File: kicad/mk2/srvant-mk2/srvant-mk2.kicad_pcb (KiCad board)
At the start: 4 copper layers, 104.8 x 158.5 mm, 241 parts, among them J1 Barrel_Jack_Switch, J10 HDMI connector, J11 USB A, J2 Conn_01x02, J3 Conn_01x03, J4 USB_OTG, J5 ARJM11, J8 Bus_M.2_Socket_M, J9 ARJM11, Q1 DMP3013SFV-7, SW1 POWER, SW2 EMMC_KEY, SW3 RST, SW4 HOST_RESET, U1 AP63205WU, U10 TPD4EUSB30, U11 TPD4EUSB30, U12 KSZ9131RNXI-TR, U13 74AHC1G04, U14 AP22653W6, U15 TLV62585DRLR, U16 FSUSB42MUX, U17 PCF85063AT/AAZ, U18 74LVC1G07SE-7, U19 TPD4EUSB30, U2 AP64501SP-13, U20 TPD4EUSB30, U21 74LVC1G07SE-7, U22 TMP1075DSG, U23 SLB9670VQ20FW785XTMA1, U24 74AHC1G08, U25 74AHC1G08, U3 74AHC1G32, U4 INA219AxDCN, U5 rp-t113-s3, U6 PCF85063AT/AAZ, U7 TPD4EUSB30, U8 74LVC2G07, U9 RT9742SNGV, Y1 X32K768S301, Y2 25Mhz, Y3 X32K768S301

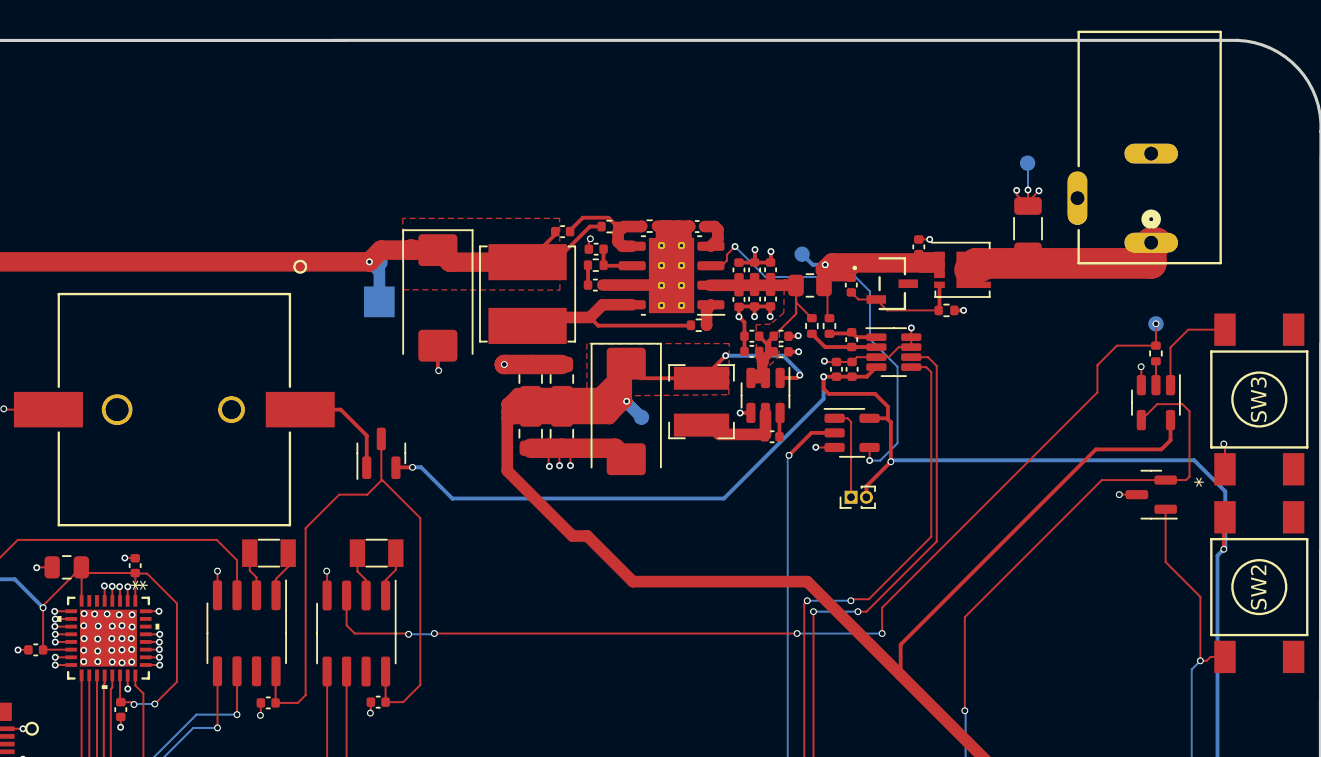
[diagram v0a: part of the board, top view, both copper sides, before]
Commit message: fix descriptions, add 3dmodels.
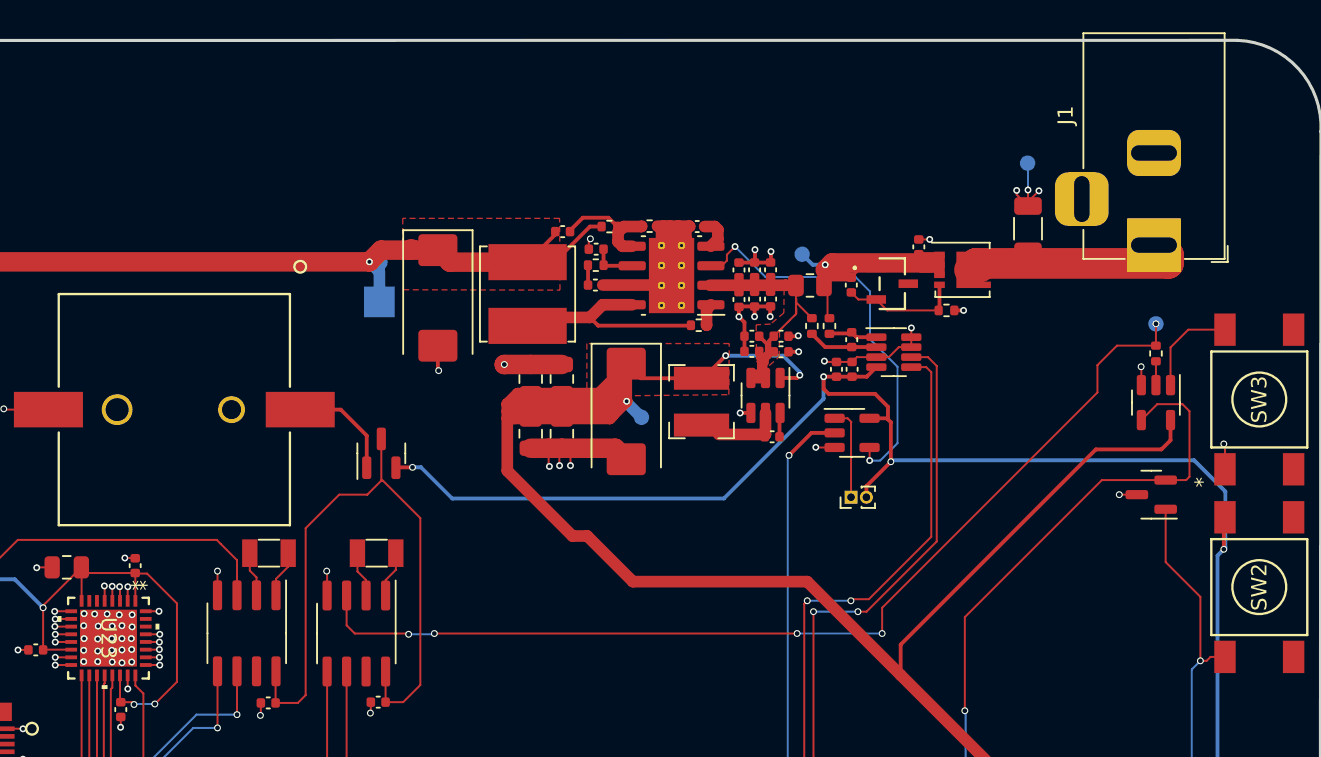
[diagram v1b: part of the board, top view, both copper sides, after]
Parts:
- J1: footprint footprints:DC-jack-694106301002 -> Connector_BarrelJack:BarrelJack_Horizontal
- SW4: value HOST_RESET -> RESET
- moved J1 0.24 mm to (105.9, 52.9)
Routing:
- net Net-(Q1-D): track 14.2 -> 15.3 mm

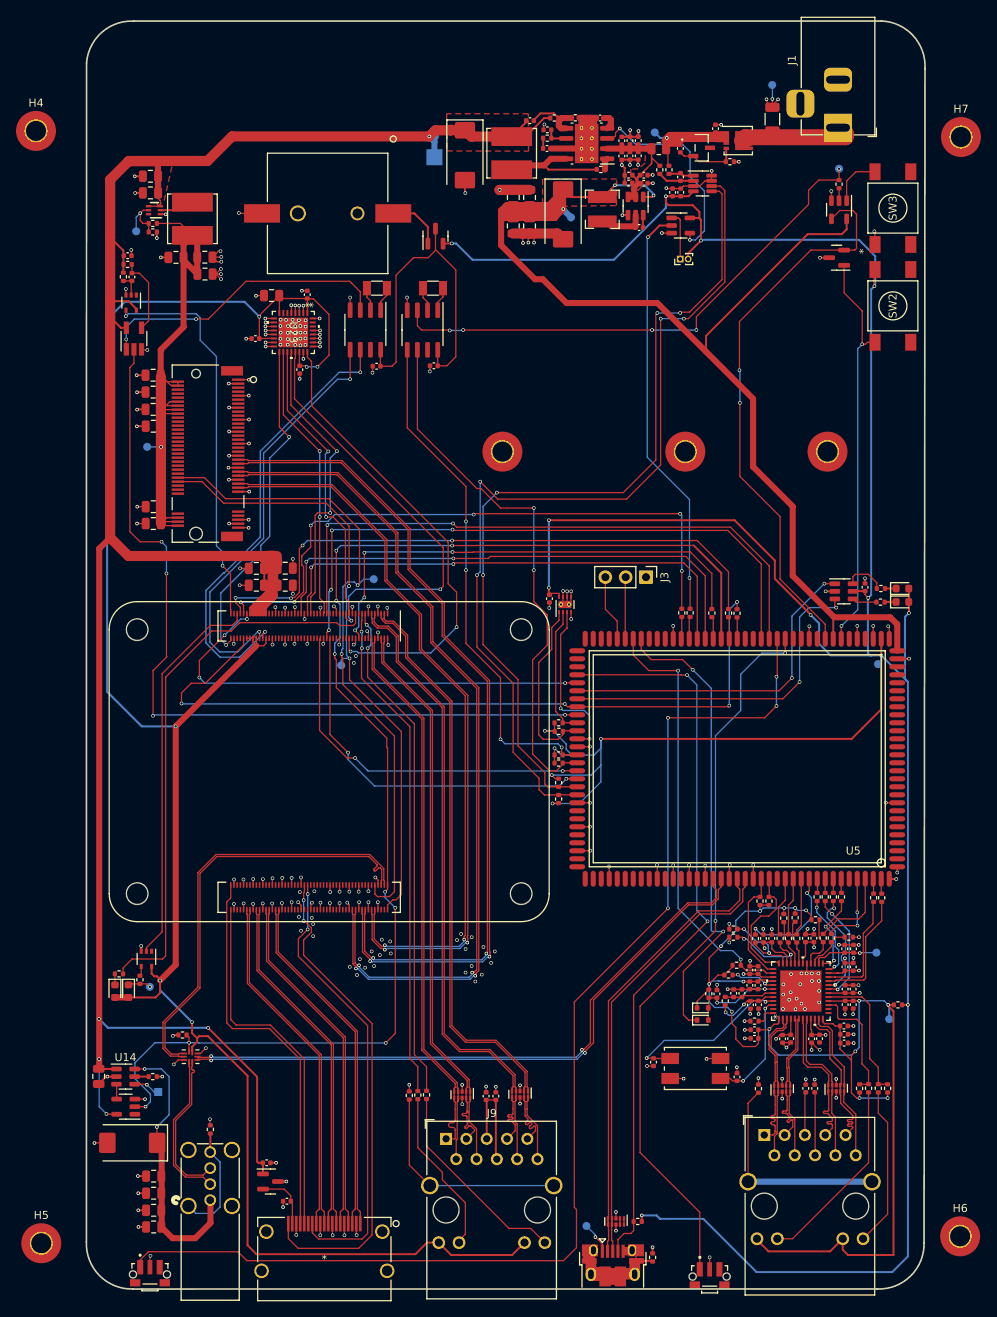
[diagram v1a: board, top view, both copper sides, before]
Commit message: replace power jack, change board dimentions, small fixes
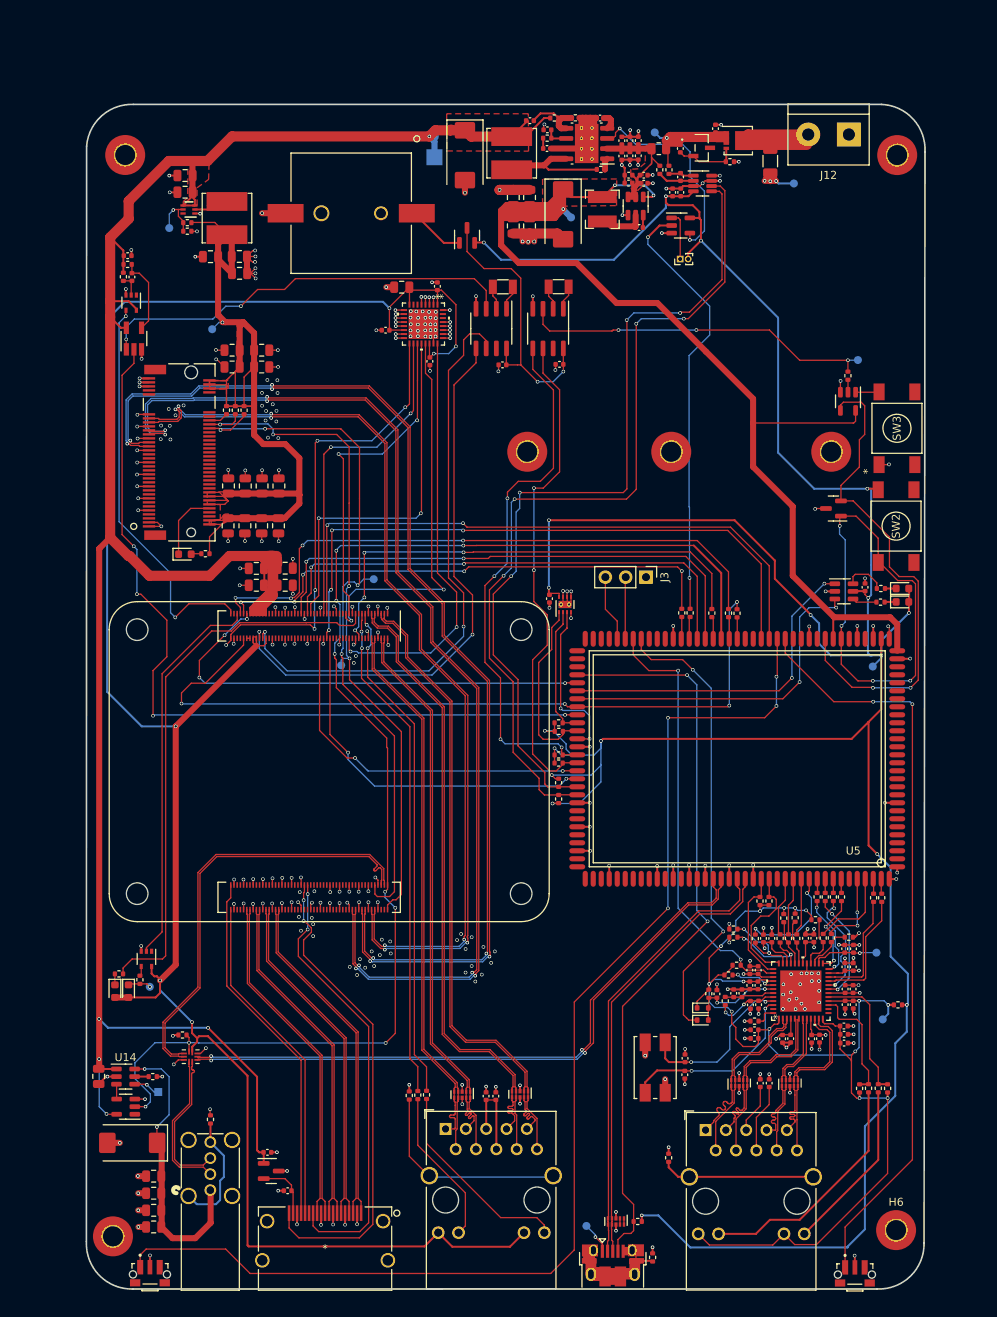
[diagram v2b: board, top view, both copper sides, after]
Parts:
- removed C100: 10u, Capacitor_SMD:C_0805_2012Metric
- removed C101, C103: 100n, Capacitor_SMD:C_0805_2012Metric
- removed J1: Barrel_Jack_Switch, Connector_BarrelJack:BarrelJack_Horizontal
- added C42: 1u, Capacitor_SMD:C_0805_2012Metric, F.Cu at (33.9, 102.7)
- added C83: 10u, Capacitor_SMD:C_0805_2012Metric, F.Cu at (36.0, 102.7)
- added C84: 1n, Capacitor_SMD:C_0805_2012Metric, F.Cu at (31.8, 102.7)
- added C85: 10u, Capacitor_SMD:C_0805_2012Metric, F.Cu at (29.8, 97.7)
- added C86: 1u, Capacitor_SMD:C_0805_2012Metric, F.Cu at (34.0, 97.7)
- added C87: 100n, Capacitor_SMD:C_0805_2012Metric, F.Cu at (36.0, 97.7)
- added C91: 1n, Capacitor_SMD:C_0805_2012Metric, F.Cu at (31.9, 97.7)
- added C92: 10u, Capacitor_SMD:C_0805_2012Metric, F.Cu at (33.9, 80.7)
- added C93: 1u, Capacitor_SMD:C_0805_2012Metric, F.Cu at (33.9, 82.8)
- added D10: LED, LED_SMD:LED_0603_1608Metric, F.Cu at (24.3, 106.2)
- added J12: Screw_Terminal_01x02, TerminalBlock:TerminalBlock_bornier-2_P5.08mm, F.Cu at (107.3, 53.7)
- added R56: 10K, Resistor_SMD:R_0402_1005Metric, F.Cu at (31.7, 88.2)
- added R61: 10K, Resistor_SMD:R_0402_1005Metric, F.Cu at (30.6, 88.2)
- added R68: 10K, Resistor_SMD:R_0402_1005Metric, F.Cu at (29.5, 88.2)
- added R74: 330R, Resistor_SMD:R_0402_1005Metric, F.Cu at (26.9, 106.1)
- C1: value 100n/100v -> 100n
- C10, C11, C12, C13, C3, C30, C33, C4, C49, C5, C52, C53, C54, C55, C56, C6, C7, C8, C9: value 10u/35v -> 10u
- C69, C71: value 10u 35v -> 10u
- C98: value 10u -> 100n
- C99: value 10u -> 1n
- R4: value 20K 1% -> 20K
- R5: value 12K 1% -> 12K
- R53: value 15K/1% -> 15K
- R54: value 100K 1% -> 100K
- R55: value 22K 1% -> 22K
- R57, R59: value 510K 1% -> 510K
- R58: value 2.2K/1% -> 2.2K
- R6: value 2.2K 1% -> 2.2K
- SW4: value RESET -> HOST_RESET
- moved D9 31.4 mm to (105.4, 100.5)
- moved SW2 27.5 mm to (113.2, 102.7)
- moved SW3 27.5 mm to (113.3, 90.5)
- moved TP19 24.0 mm to (108.4, 81.9)
- moved R73 24.0 mm to (107.2, 83.9)
- moved U25 24.0 mm to (107.2, 87.1)
- moved C99 21.9 mm to (30.2, 82.8)
- moved C98 21.9 mm to (30.2, 80.7)
- moved J8 19.1 mm to (27.4, 84.2), turned to 90 degrees
- moved SW1 18.2 mm to (108.0, 196.2)
- moved TP12 16.8 mm to (27.7, 78.1)
- moved C94 16.3 mm to (51.4, 72.8)
- moved C95 16.3 mm to (55.9, 72.7)
- moved C96 16.3 mm to (54.9, 82.1)
- moved C97 16.3 mm to (49.4, 78.2)
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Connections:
- net Net-(Q1-D) renamed /power/VIN
- J8 pad 10: unconnected-(J8-DAS/~DSS~/~LED1-Pad10) -> Net-(D10-K)
- J8 pad 54: unconnected-(J8-~PEWAKE-Pad54) -> /cm4/PCIE_WAKE
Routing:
- net /cm4/+3.3v_HOST_PCIe: track 77.6 -> 138.9 mm
- net /cm4/PCIE_RX_N: track 104.8 -> 139.3 mm, vias 2 -> 4
- net /cm4/PCIE_RX_P: track 103.3 -> 137.0 mm, vias 2 -> 4
- net /cm4/PCIE_TX_N: track 106.8 -> 137.4 mm, vias 2 -> 4
- net /BMC ethernet/3.3v_BMC: track 402.1 -> 371.8 mm, vias 17 -> 18
- net /cm4/PCIE_TX_P: track 105.7 -> 135.3 mm, vias 2 -> 4
- net /cm4/PCIE_CLK_N: track 92.7 -> 117.4 mm, vias 2 -> 4
- net /cm4/PCIE_CLK_P: track 91.2 -> 115.5 mm, vias 2 -> 4
- net /bmc/NMI_N: track 66.1 -> 44.7 mm, vias 5 -> 3
- net /cm4/HOST_SDA0: track 53.3 -> 70.9 mm
- net /cm4/HOST_SCL0: track 56.6 -> 73.9 mm
- net /cm4/nRTC_INT: track 37.3 -> 53.2 mm
- net /cm4/nEXTRST: track 42.0 -> 57.4 mm, vias 2 -> 5
- net /cm4/+3.3v_HOST: track 248.0 -> 262.8 mm
- net GND: track 301.6 -> 316.2 mm, vias 314 -> 320
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- added copper zone on F.Cu, net /cm4/+3.3v_HOST_PCIe
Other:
- board size 104.8 x 158.5 mm -> 104.8 x 148.1 mm

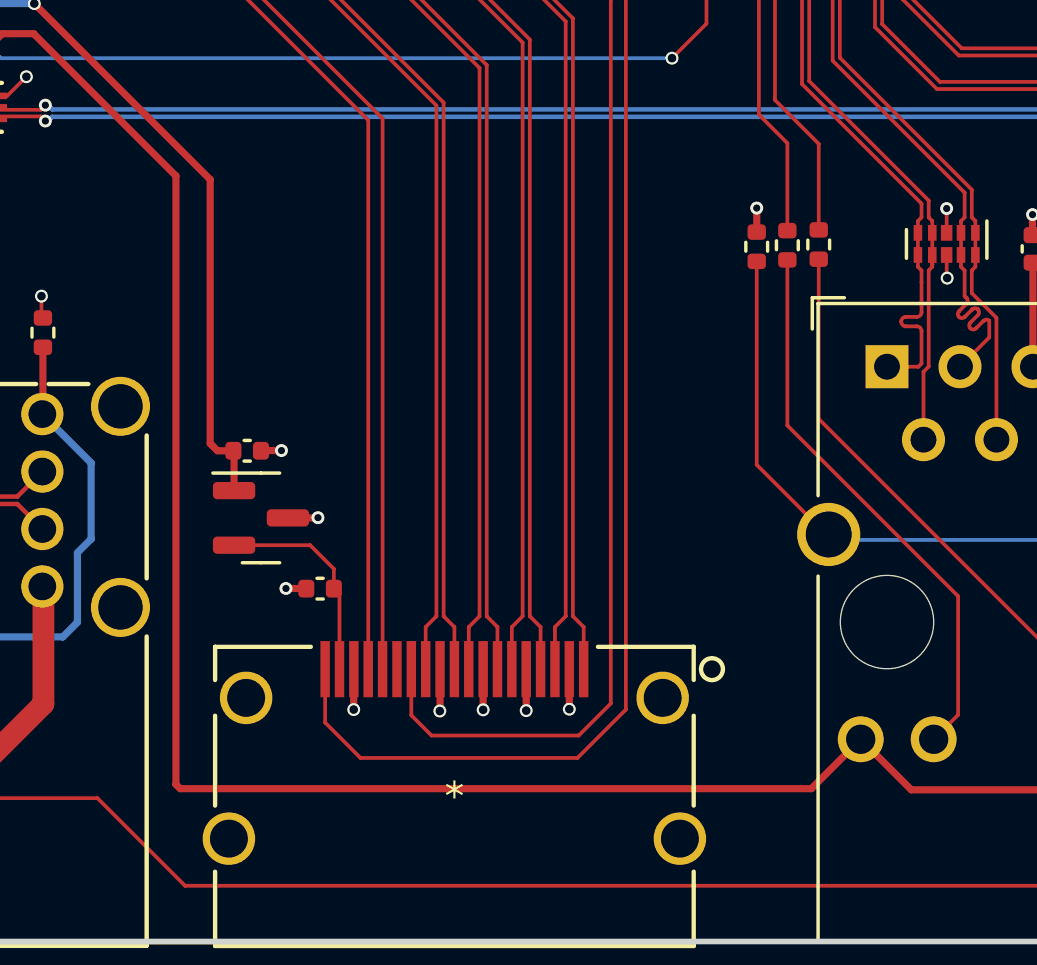
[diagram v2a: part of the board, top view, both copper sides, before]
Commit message: add more 3d models
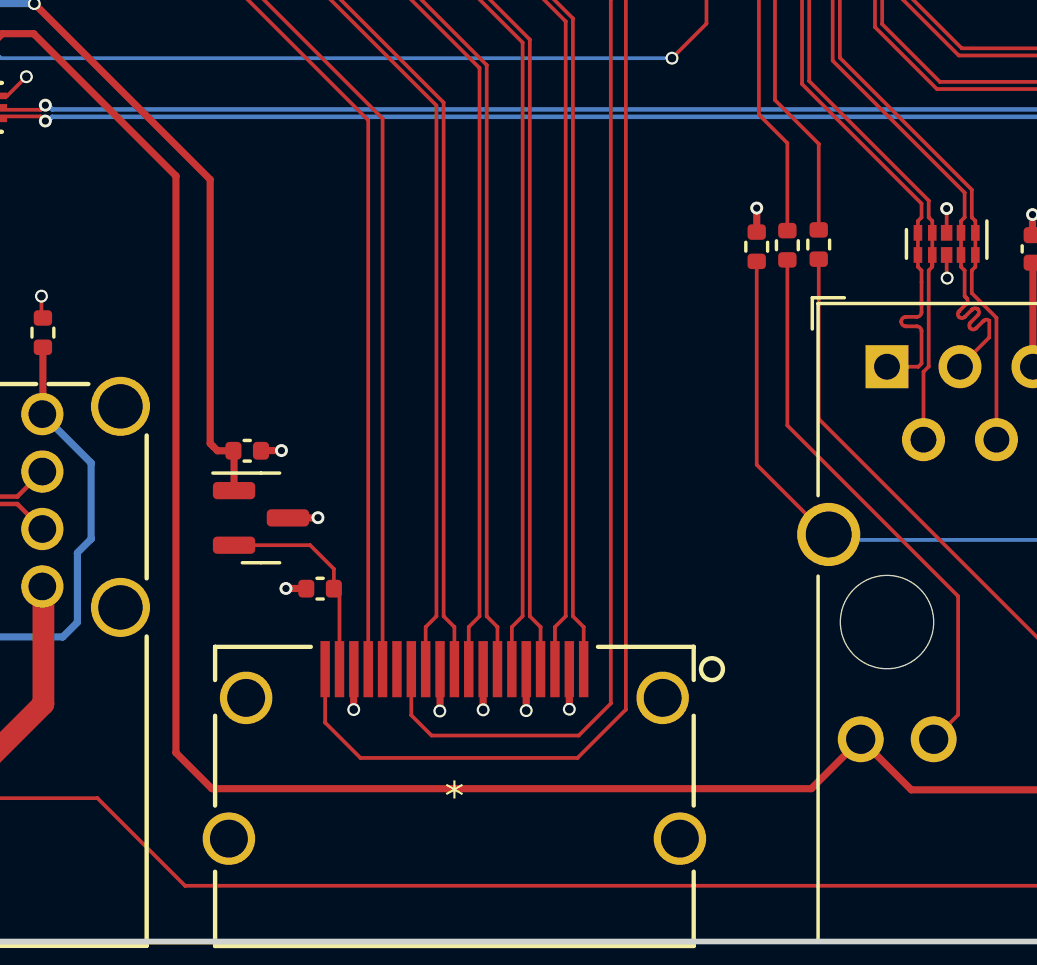
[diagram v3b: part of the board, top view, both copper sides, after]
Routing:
- net /cm4/+3.3v_HOST: track 262.8 -> 262.1 mm

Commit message: add more 3d models, add layer indication, update readme
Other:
- board text added: "A"
- board text added: "B"
- board text added: "C"
- board text added: "D"
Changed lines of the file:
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@@
     (pad "7" thru_hole circle (at -2.72 -6.27) (size 2.0574 2.0574) (drill 1.5494) (layers "*.Cu" "*.Mask"))
     (pad "8" thru_hole circle (at 2.72 -6.27) (size 2.0574 2.0574) (drill 1.5494) (layers "*.Cu" "*.Mask"))
+    (model "${MK2_3D_MODELS}/usb-vertical-c-292336-1-b-3d.stp"
+      (offset (xyz 0 -12.5 7))
+      (scale (xyz 1 1 1))
+      (rotate (xyz 0 -90 90))
+    )
   )
   (footprint "footprints:FSUSB42UMX" (layer "F.Cu")
@@
           (width 0) (fill yes))
       ))
-    (model "${KICAD7_3DMODEL_DIR}/Package_SON.3dshapes/Diodes_PowerDI3333-8.wrl"
+    (model "${MK2_3D_MODELS}/POWERDI3333-8_UX_DIO.step"
       (offset (xyz 0 0 0))
       (scale (xyz 1 1 1))
@@
     )
   )
+  (gr_text "A" (at 114.68 62.69) (layer "F.Cu")
+    (effects (font (size 1 1)) (justify left bottom))
+  )
+  (gr_text "B" (at 114.59 64.57) (layer "In1.Cu")
+    (effects (font (size 1 1)) (justify left bottom))
+  )
+  (gr_text "C" (at 114.58 66.35) (layer "In2.Cu")
+    (effects (font (size 1 1)) (justify left bottom))
+  )
+  (gr_text "D" (at 114.66 68.15) (layer "B.Cu")
+    (effects (font (size 1 1)) (justify left bottom))
+  )
   (via (at 35.88 86.05) (size 0.45) (drill 0.3) (layers "F.Cu" "B.Cu") (net 0))
   (via (at 34.39 89.49) (size 0.45) (drill 0.3) (layers "F.Cu" "B.Cu") (net 0))
@@
       )
     )
+  )
+  (zone (net 0) (net_name "") (layers "F.Cu" "In1.Cu") (hatch none 0.5)
+    (connect_pads (clearance 0))
+    (min_thickness 0.25) (filled_areas_thickness no)
+    (keepout (tracks not_allowed) (vias not_allowed) (pads not_allowed) (copperpour not_allowed) (footprints not_allowed))
+    (fill (thermal_gap 0.5) (thermal_bridge_width 0.5))
+    (polygon
+      (pts
+        (xy 114.47 63.08)
+        (xy 115.77 63.08)
+        (xy 115.77 64.88)
+        (xy 114.47 64.88)
+      )
+    )
+  )
+  (zone (net 0) (net_name "") (layers "F.Cu" "In1.Cu" "In2.Cu") (hatch none 0.5)
+    (connect_pads (clearance 0))
+    (min_thickness 0.25) (filled_areas_thickness no)
+    (keepout (tracks not_allowed) (vias not_allowed) (pads not_allowed) (copperpour not_allowed) (footprints not_allowed))
+    (fill (thermal_gap 0.5) (thermal_bridge_width 0.5))
+    (polygon
+      (pts
+        (xy 114.47 64.88)
+        (xy 115.77 64.88)
+        (xy 115.77 66.68)
+        (xy 114.47 66.68)
+      )
+    )
+  )
+  (zone (net 0) (net_name "") (layers "F.Cu" "In1.Cu" "In2.Cu" "B.Cu") (hatch none 0.5)
+    (connect_pads (clearance 0))
+    (min_thickness 0.25) (filled_areas_thickness no)
+    (keepout (tracks not_allowed) (vias not_allowed) (pads not_allowed) (copperpour not_allowed) (footprints not_allowed))
+    (fill (thermal_gap 0.5) (thermal_bridge_width 0.5))
+    (polygon
+      (pts
+        (xy 114.47 61.28)
+        (xy 115.77 61.28)
+        (xy 115.77 63.08)
+        (xy 114.47 63.08)
+      )
+    )
+  )
+  (zone (net 0) (net_name "") (layers "F.Cu" "In1.Cu" "In2.Cu" "B.Cu") (hatch none 0.5)
+    (connect_pads (clearance 0))
+    (min_thickness 0.25) (filled_areas_thickness no)
+    (keepout (tracks not_allowed) (vias not_allowed) (pads not_allowed) (copperpour not_allowed) (footprints not_allowed))
+    (fill (thermal_gap 0.5) (thermal_bridge_width 0.5))
+    (polygon
+      (pts
+        (xy 114.47 66.68)
+        (xy 115.77 66.68)
+        (xy 115.77 68.48)
+        (xy 114.47 68.48)
+      )
+    )
